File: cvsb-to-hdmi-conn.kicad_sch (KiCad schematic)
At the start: 25 parts

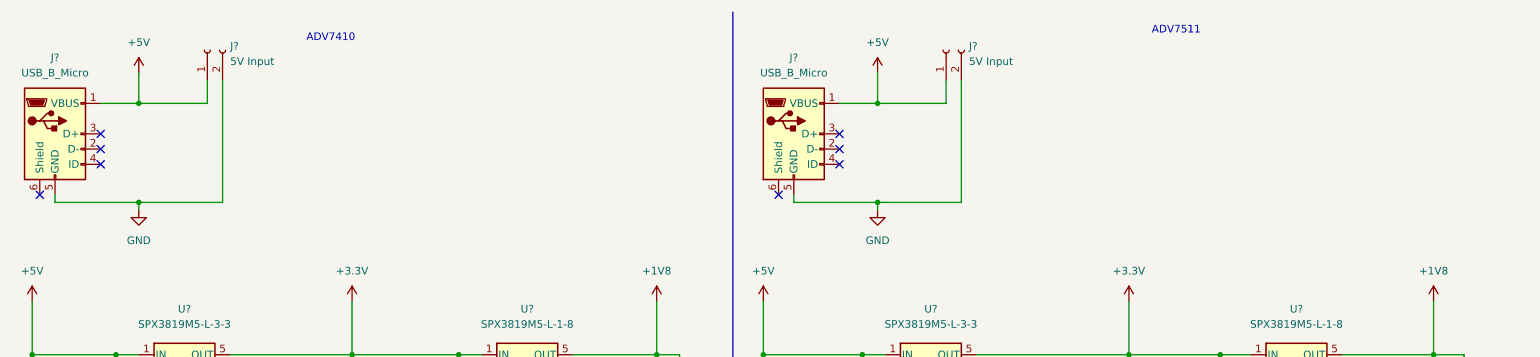
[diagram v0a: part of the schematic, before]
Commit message: Add overvoltage and overcurrent protection elements
And LEDs to the power indication
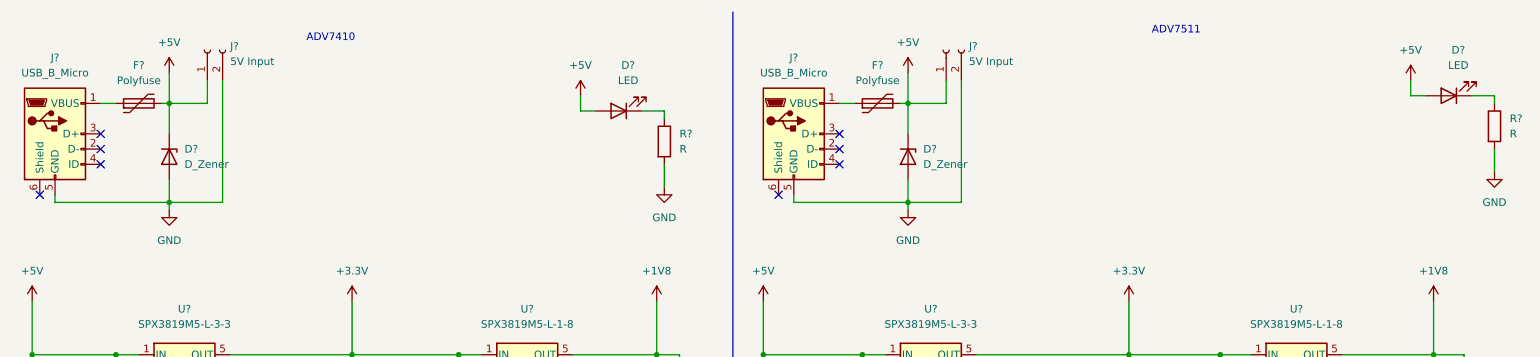
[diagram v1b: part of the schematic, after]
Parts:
- added D? (x2): LED, symbol Device:LED
- added D? (x2): D_Zener, symbol Device:D_Zener
- added F? (x2): Polyfuse, symbol Device:Polyfuse
- added R? (x2): R, symbol Device:R
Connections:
- net +5V: now also D?.1 (K), D?.1 (K), D?.2 (A), D?.2 (A), F?.2, F?.2; no longer J?.1 (VBUS), J?.1 (VBUS)
- net GND: now also D?.2 (A), D?.2 (A), R?.2, R?.2
- new net: D?.1 (K), R?.1 (x2)
- new net: F?.1, J?.1 (VBUS) (x2)

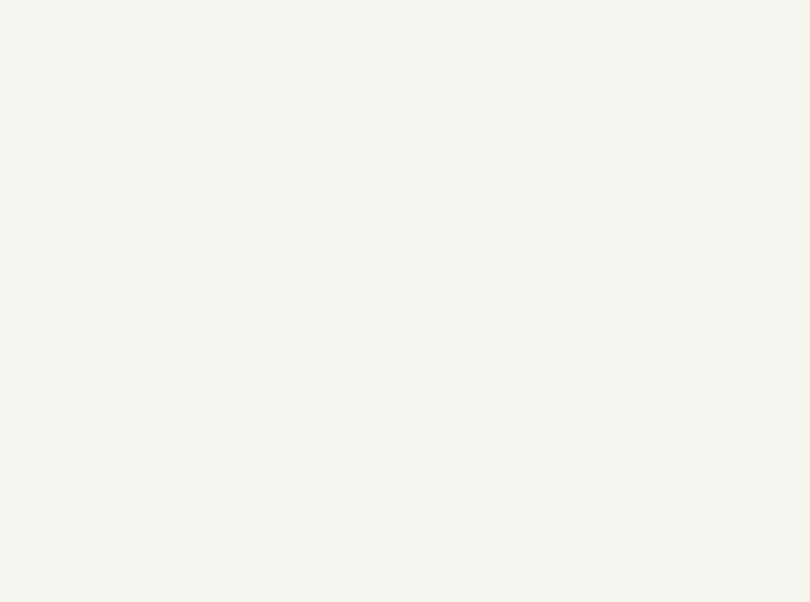
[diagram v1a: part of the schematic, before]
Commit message: Add symbol to library
Not full symbol, only few pins
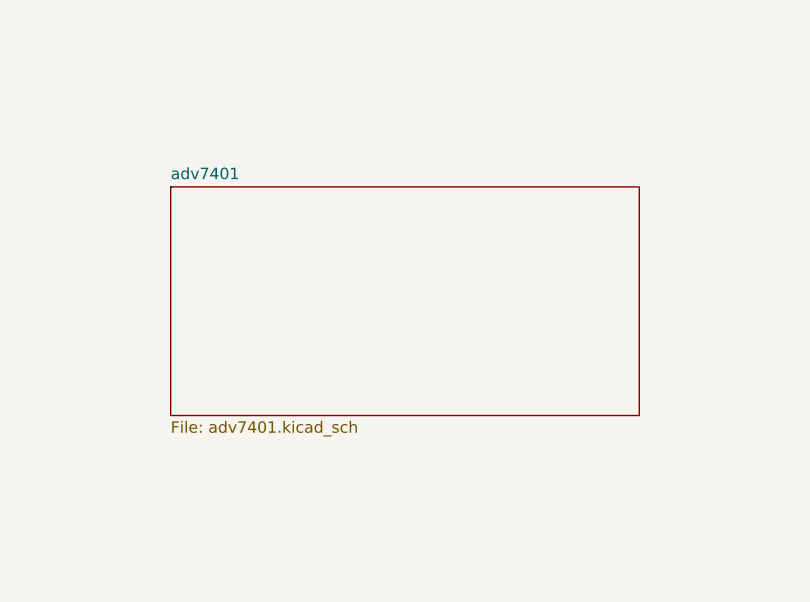
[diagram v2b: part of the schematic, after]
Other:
- added sheet adv7401 (adv7401.kicad_sch)
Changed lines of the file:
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@@
     (pin "1")
+  )
+  (sheet (at 54.61 142.24) (size 52.07 25.4) (fields_autoplaced)
+    (stroke (width 0.1524) (type solid) (color 0 0 0 0))
+    (fill (color 0 0 0 0.0000))
+    (property "Sheet name" "adv7401" (id 0) (at 54.61 141.5284 0)
+      (effects (font (size 1.27 1.27)) (justify left bottom))
+    )
+    (property "Sheet file" "adv7401.kicad_sch" (id 1) (at 54.61 168.2246 0)
+      (effects (font (size 1.27 1.27)) (justify left top))
+    )
   )
   (sheet_instances
     (path "/" (page "1"))
+    (path "/5674e1dc-71af-4906-a3b6-be98e2c5093c" (page "2"))
   )
   (symbol_instances
